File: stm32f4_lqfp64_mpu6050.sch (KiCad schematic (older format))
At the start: 0 parts

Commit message: added lots of stuff
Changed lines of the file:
@@
 EESchema Schematic File Version 2
+LIBS:stm32f4_lqfp64_mpu6050-rescue
 LIBS:power
 LIBS:device
@@
 LIBS:minimal
 LIBS:alis_parts
+LIBS:sensors
+LIBS:stm32
 LIBS:stm32f4_lqfp64_mpu6050-cache
 EELAYER 25 0
@@
 $Descr A4 11693 8268
 encoding utf-8
-Sheet 1 7
+Sheet 1 10
 Title ""
 Date ""
@@
 F1 "ublox_neo7.sch" 60
 $EndSheet
+$Sheet
+S 3800 700  850  700
+U 5698CFC3
+F0 "hmc5884l" 60
+F1 "hmc5883l.sch" 60
+$EndSheet
+$Sheet
+S 3800 1750 850  700
+U 569B6D4A
+F0 "bmp180" 60
+F1 "bmp180.sch" 60
+$EndSheet
+$Sheet
+S 4800 700  850  700
+U 569F55FA
+F0 "mic5205" 60
+F1 "mic5205.sch" 60
+$EndSheet
 $EndSCHEMATC

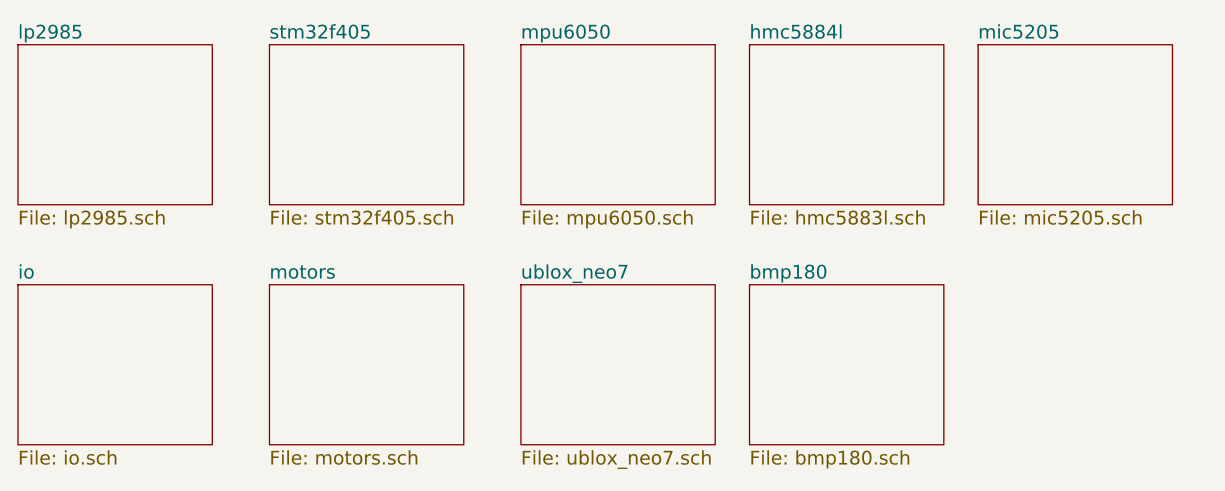
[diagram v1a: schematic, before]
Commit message: began to add support for video overlay
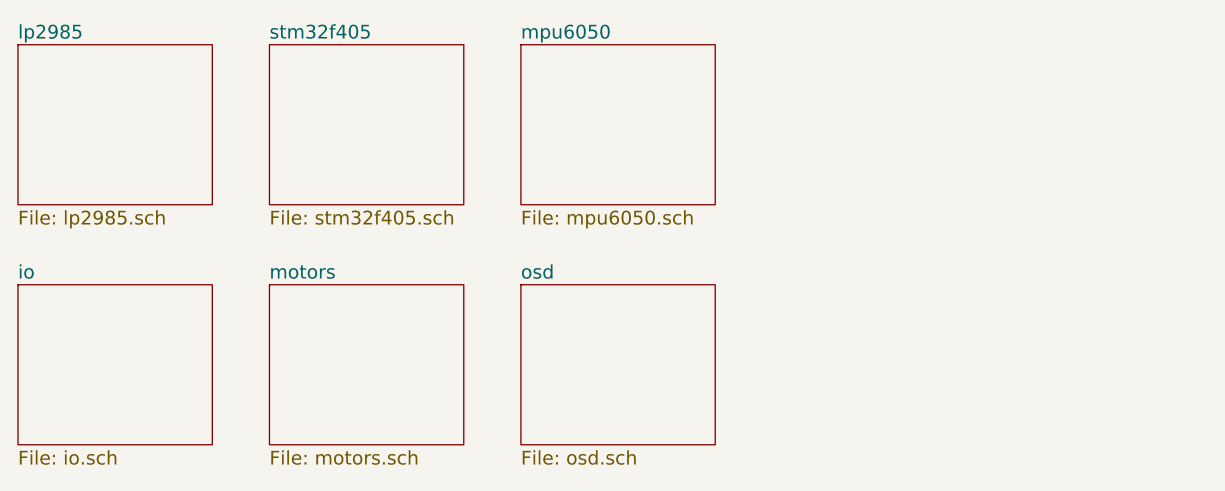
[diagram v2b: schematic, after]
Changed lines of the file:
@@
 $Descr A4 11693 8268
 encoding utf-8
-Sheet 1 10
+Sheet 1 7
 Title ""
 Date ""
@@
 $Sheet
 S 2800 1750 850  700
-U 5698349A
-F0 "ublox_neo7" 60
-F1 "ublox_neo7.sch" 60
-$EndSheet
-$Sheet
-S 3800 700  850  700
-U 5698CFC3
-F0 "hmc5884l" 60
-F1 "hmc5883l.sch" 60
-$EndSheet
-$Sheet
-S 3800 1750 850  700
-U 569B6D4A
-F0 "bmp180" 60
-F1 "bmp180.sch" 60
-$EndSheet
-$Sheet
-S 4800 700  850  700
-U 569F55FA
-F0 "mic5205" 60
-F1 "mic5205.sch" 60
+U 57069947
+F0 "osd" 60
+F1 "osd.sch" 60
 $EndSheet
 $EndSCHEMATC

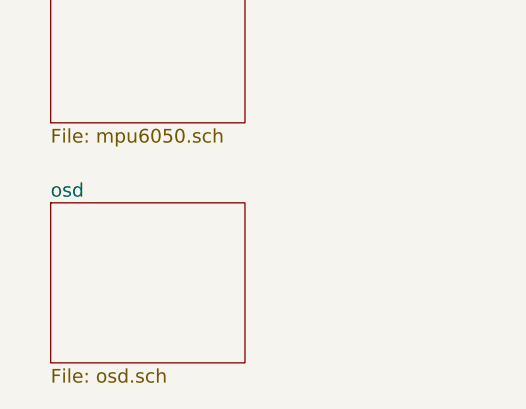
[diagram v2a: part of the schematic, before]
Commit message: power traces routed
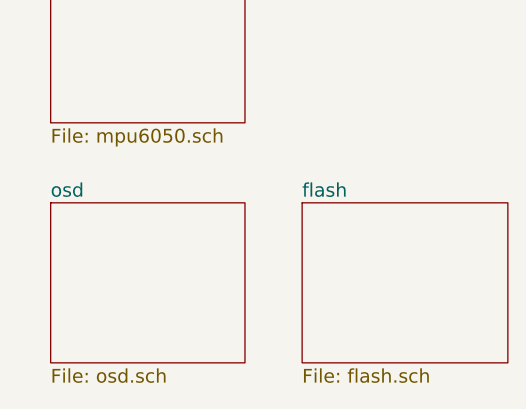
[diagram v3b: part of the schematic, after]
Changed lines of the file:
@@
 $Descr A4 11693 8268
 encoding utf-8
-Sheet 1 7
+Sheet 1 8
 Title ""
 Date ""
@@
 F0 "io" 60
 F1 "io.sch" 60
-$EndSheet
-$Sheet
-S 1700 1750 850  700
-U 56980F2E
-F0 "motors" 60
-F1 "motors.sch" 60
 $EndSheet
 $Sheet
@@
 F1 "osd.sch" 60
 $EndSheet
+$Sheet
+S 1700 1750 850  700
+U 56980F2E
+F0 "motors" 60
+F1 "motors.sch" 60
+$EndSheet
+$Sheet
+S 3900 1750 900  700
+U 5729526E
+F0 "flash" 60
+F1 "flash.sch" 60
+$EndSheet
 $EndSCHEMATC
